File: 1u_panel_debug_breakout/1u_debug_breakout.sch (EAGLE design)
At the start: 12 parts, among them J1 1.27MM-SWD-CONNECTOR, SW1 1825910-6

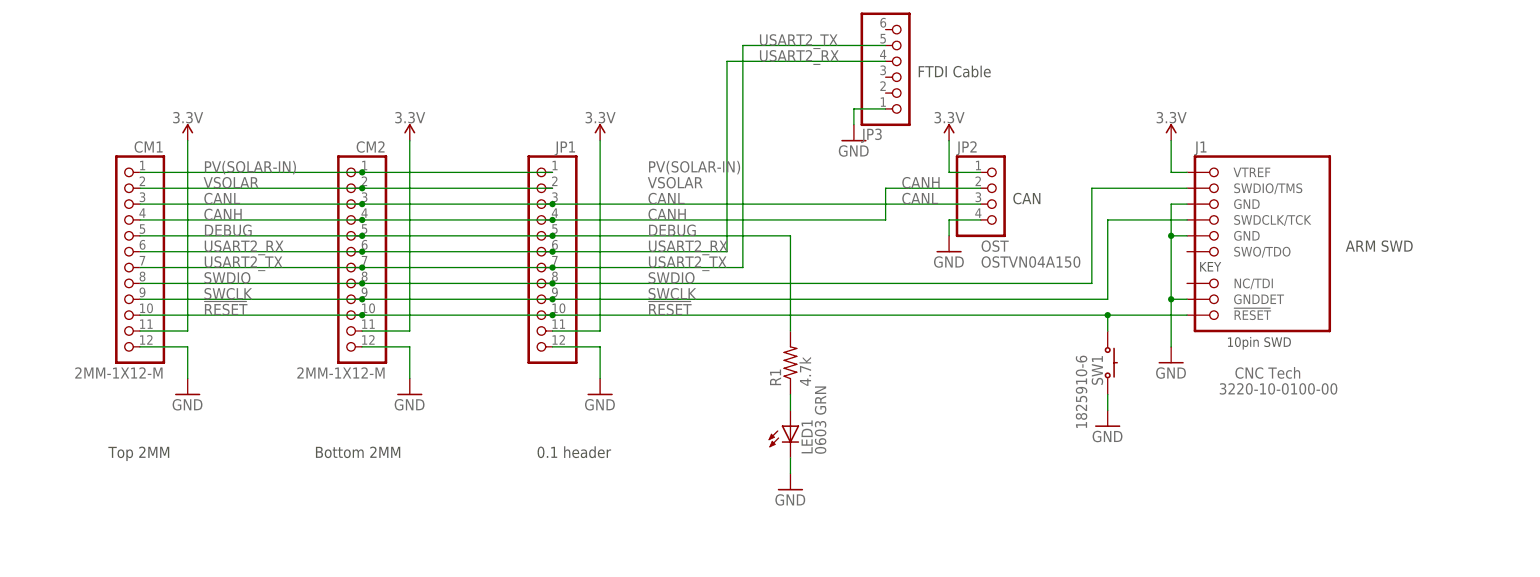
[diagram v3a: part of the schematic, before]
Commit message: updated FFC debug breakout
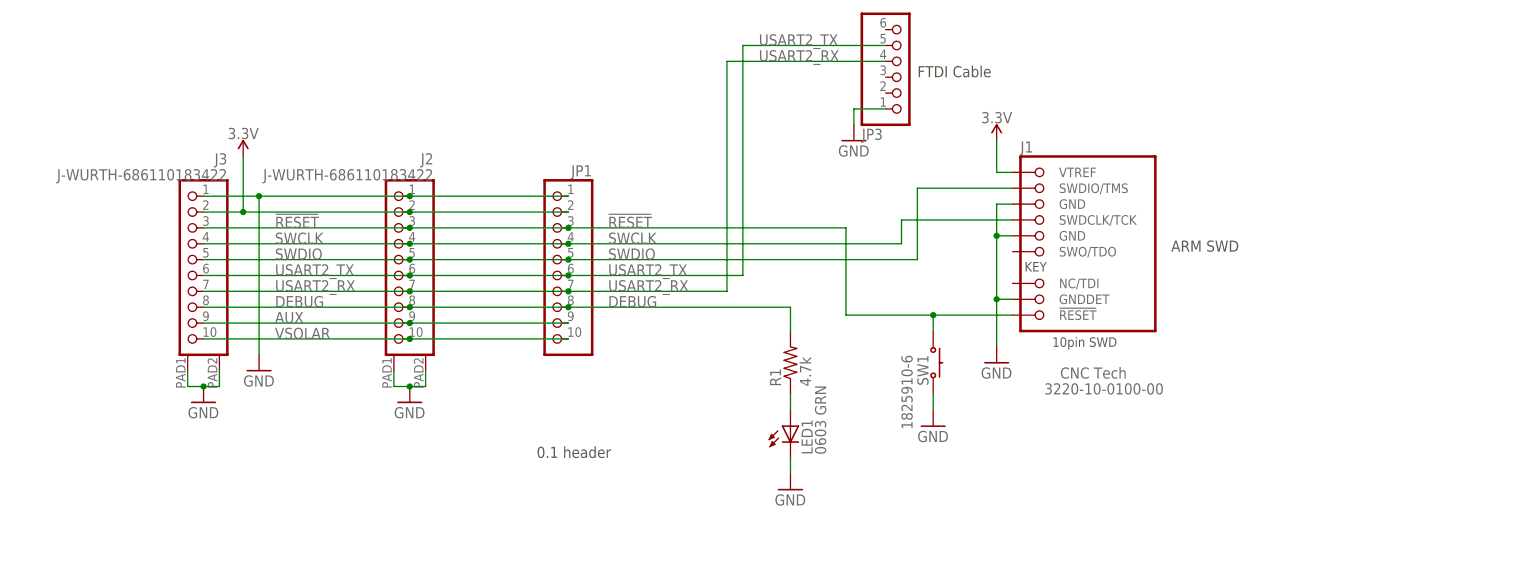
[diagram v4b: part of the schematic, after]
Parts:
- removed CM1, CM2: 2MM-1X12-M, J-precidip-880-2mm:2MM-1X12-M
- removed JP2: (no value), pinhead:PINHD-1X4
- added J2, J3: J-WURTH-686110183422, J-Wurth-686110183422-10pos-FFC:J-WURTH-686110183422
- JP1: device pinhead:PINHD-1X12 -> pinhead:PINHD-1X10
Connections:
- removed net CANH: CM1.4, CM2.4, JP1.4, JP2.2
- removed net CANL: CM1.3, CM2.3, JP1.3, JP2.3
- removed net PV(SOLAR-IN): CM1.1, CM2.1, JP1.1
- new net AUX: J2.9, J3.9, JP1.9
- net !RESET: now also J2.3, J3.3, JP1.3; no longer CM1.10, CM2.10, JP1.10
- net 3.3V: now also J2.2, J3.2, JP1.2; no longer CM1.11, CM2.11, JP1.11, JP2.1
- net DEBUG: now also J2.8, J3.8, JP1.8; no longer CM1.5, CM2.5, JP1.5
- net GND: now also J2.1, J2.PAD1, J2.PAD2, J3.1, J3.PAD1, J3.PAD2, JP1.1; no longer CM1.12, CM2.12, JP1.12, JP2.4
- net SWCLK: now also J2.4, J3.4, JP1.4; no longer CM1.9, CM2.9, JP1.9
- net SWDIO: now also J2.5, J3.5, JP1.5; no longer CM1.8, CM2.8, JP1.8
- net USART2_RX: now also J2.7, J3.7, JP1.7; no longer CM1.6, CM2.6, JP1.6
- net USART2_TX: now also J2.6, J3.6, JP1.6; no longer CM1.7, CM2.7, JP1.7
- net VSOLAR: now also J2.10, J3.10, JP1.10; no longer CM1.2, CM2.2, JP1.2
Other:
- note removed: "Bottom 2MM"
- note removed: "CAN"
- note removed: "Top 2MM"
- moved on the sheet: J1, SW1
